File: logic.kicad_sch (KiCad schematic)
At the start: 38 parts, among them J2 TC2030, J5 Conn_01x04_Pin, J8 Conn_01x04, J9 Conn_01x04, SW1 SW_Push, SW2 SW_Push, U2 SN65HVD230, U4 HT753-1, U6 STM32F103C8Tx, Y1 8M

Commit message: schem: update 6n conn tvs diodes
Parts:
- removed D8, D9: H5VU10U, GLCS:Diode_DFN1006, symbol GLCS:H5VU10U
- added D17, D18: SMBJ6.0CA, Diode_SMD:D_SMA, symbol Device:D_TVS
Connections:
- net +5V: now also D17.1 (A1), D18.1 (A1)
- net GND: now also D17.2 (A2), D18.2 (A2)

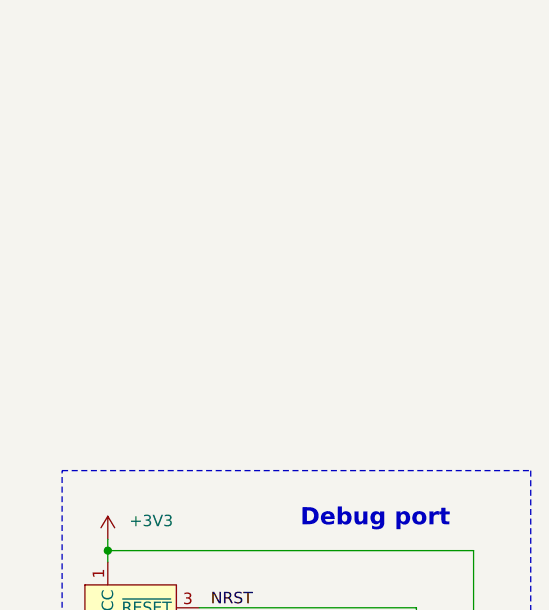
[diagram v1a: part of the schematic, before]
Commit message: schem: add rgb status led
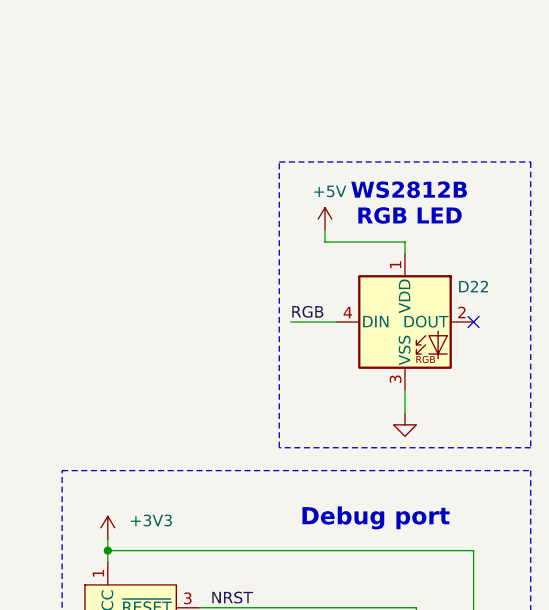
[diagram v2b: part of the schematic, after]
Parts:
- added D22: WS2812B, LED_SMD:LED_WS2812B_PLCC4_5.0x5.0mm_P3.2mm, symbol LED:WS2812B
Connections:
- net +5V: now also D22.1 (VDD)
- net GND: now also D22.3 (VSS)
- new net RGB: D22.4 (DIN)
- no-connect marks 3 -> 4
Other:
- note added: "WS2812B RGB LED"

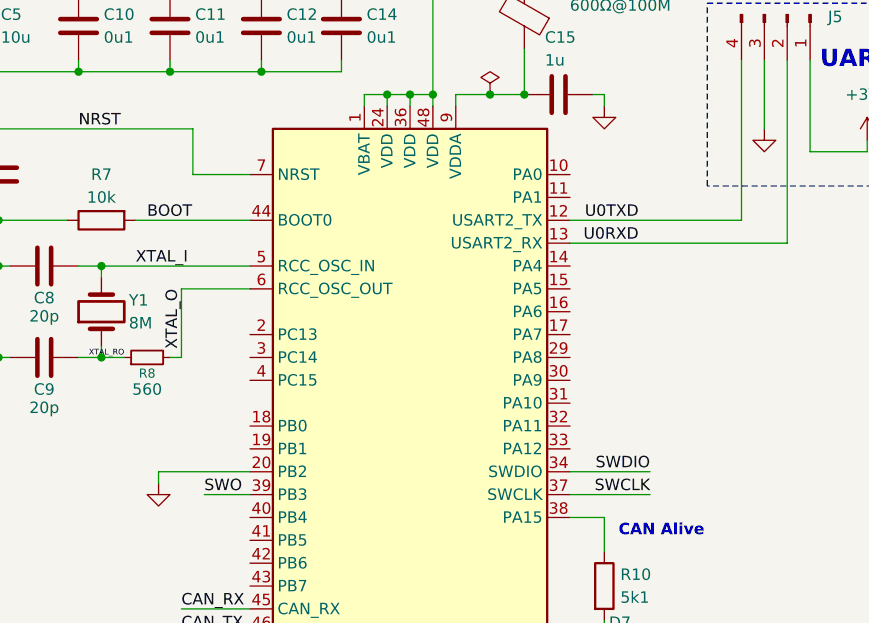
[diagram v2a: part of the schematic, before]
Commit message: schem: connect efuses to mcu
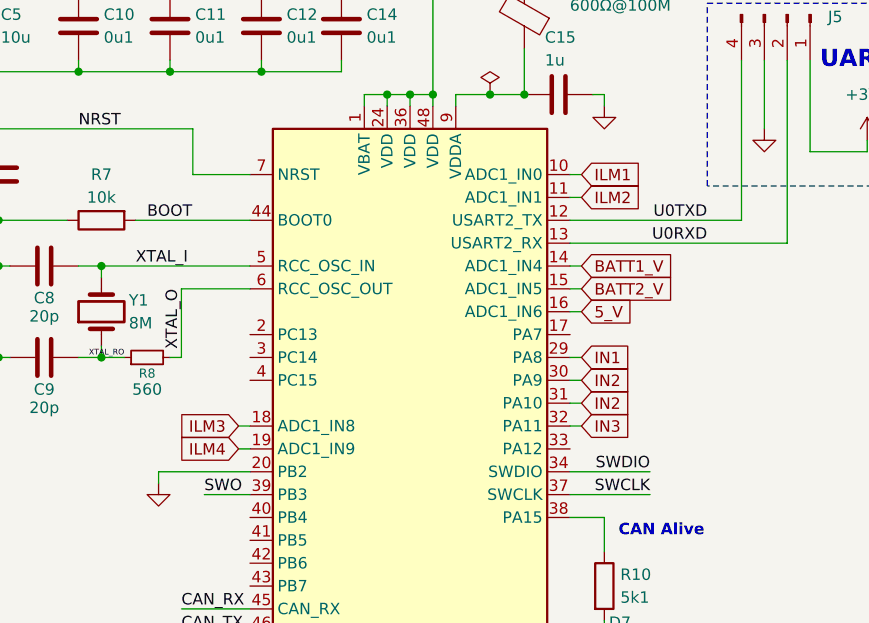
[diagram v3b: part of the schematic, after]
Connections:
- net ILM1: now reaches U6.10 (PA0)
- net ILM2: now reaches U6.11 (PA1)
- net BATT1_V: now reaches U6.14 (PA4)
- net BATT2_V: now reaches U6.15 (PA5)
- net 5_V: now reaches U6.16 (PA6)
- net ILM3: now reaches U6.18 (PB0)
- net ILM4: now reaches U6.19 (PB1)
- net IN1: now reaches U6.29 (PA8)
- net IN2: now reaches U6.30 (PA9)
- net IN2: now also U6.31 (PA10)
- net IN3: now reaches U6.32 (PA11)

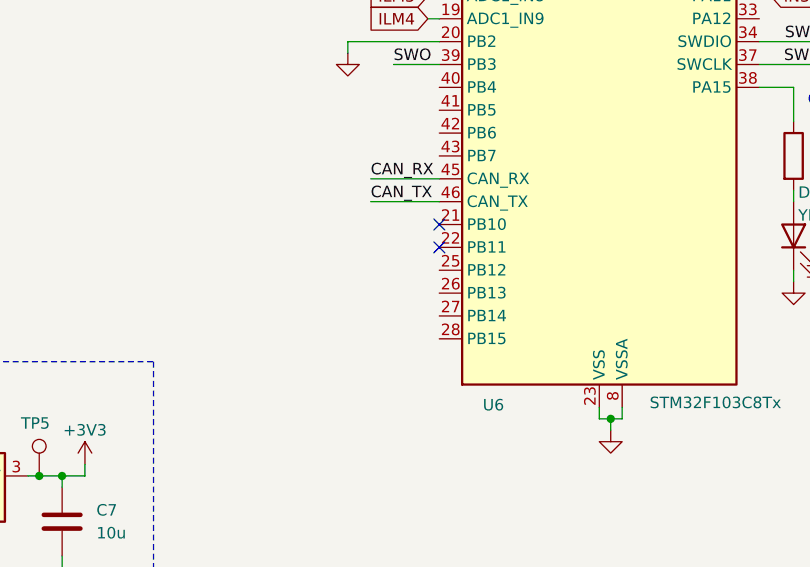
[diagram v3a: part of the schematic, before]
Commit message: schem: add test points
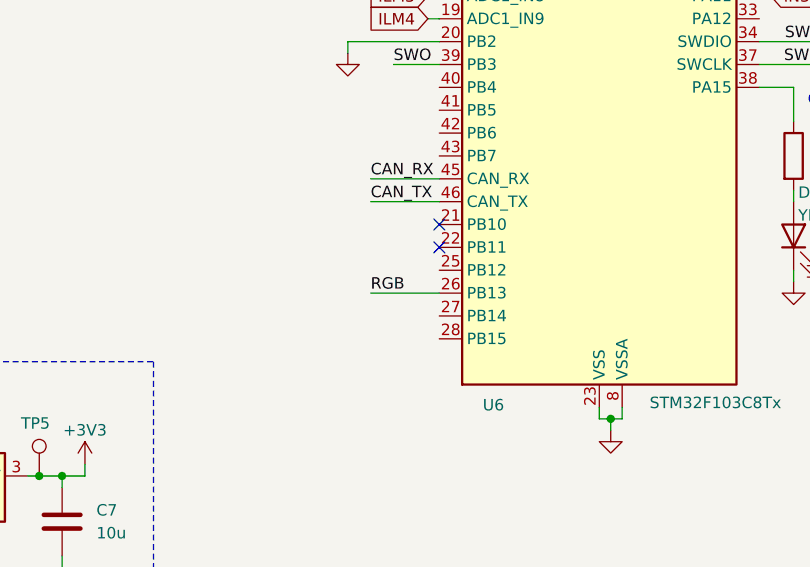
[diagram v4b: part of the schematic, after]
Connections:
- net RGB: now also U6.26 (PB13)
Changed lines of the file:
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@@
+	(wire
+		(pts
+			(xy 116.84 123.19) (xy 124.46 123.19)
+		)
+		(stroke
+			(width 0)
+			(type default)
+		)
+	)
 	(wire
 		(pts
@@
 		)
 	)
+	(label "RGB"
+		(at 116.84 123.19 0)
+		(effects
+			(font
+				(size 1.27 1.27)
+			)
+			(justify left bottom)
+		)
+	)

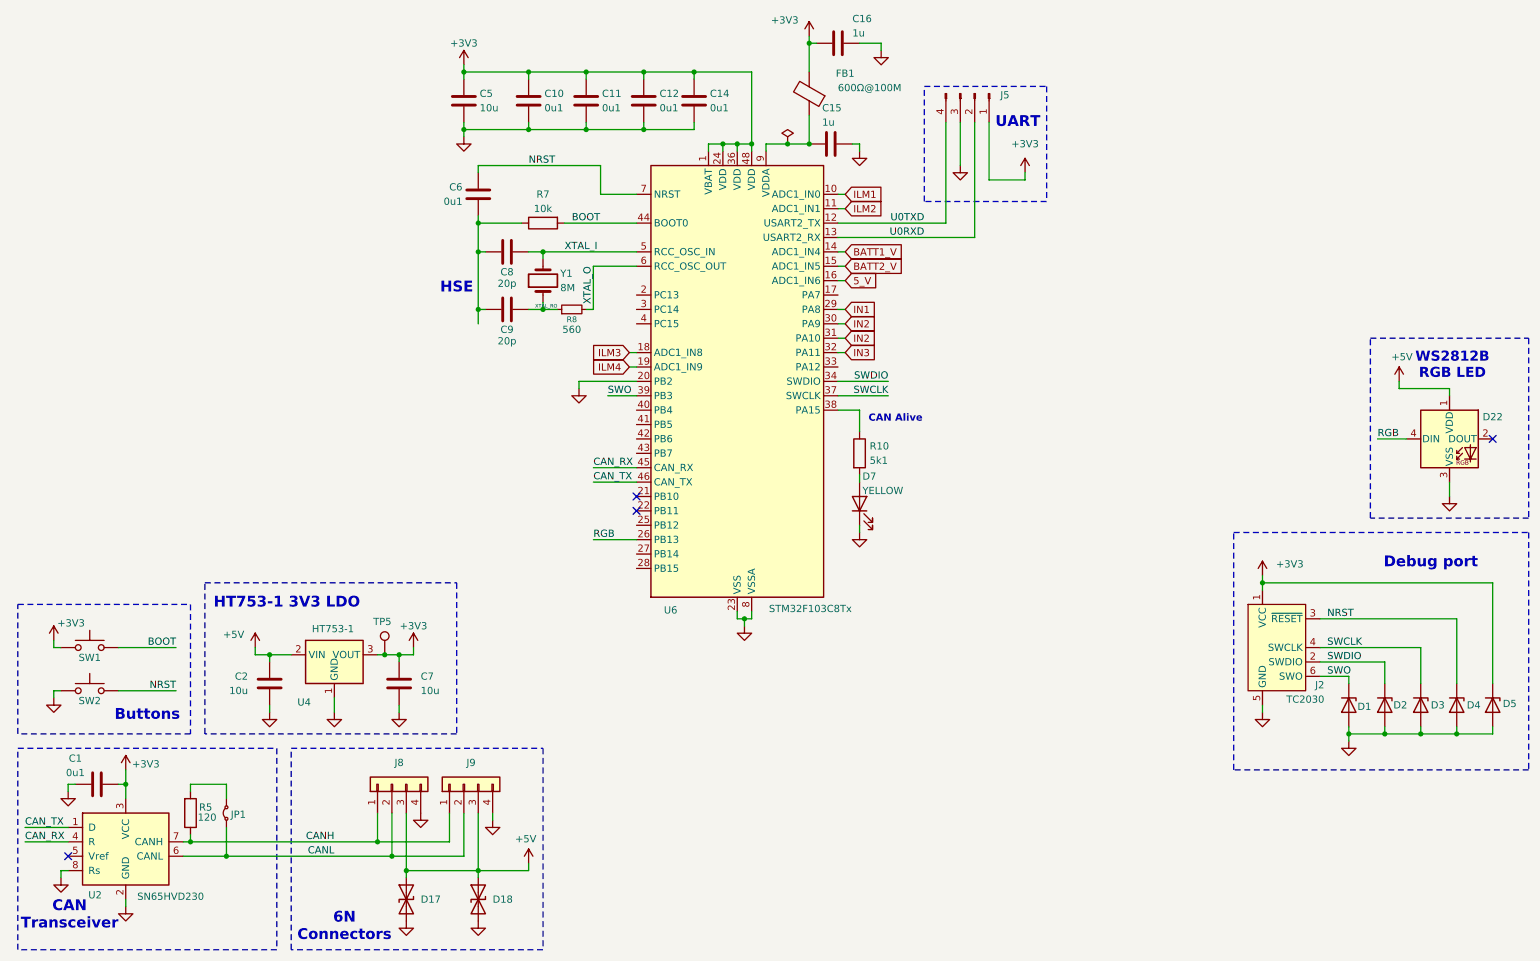
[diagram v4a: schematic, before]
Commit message: schem: add current measure jumpers
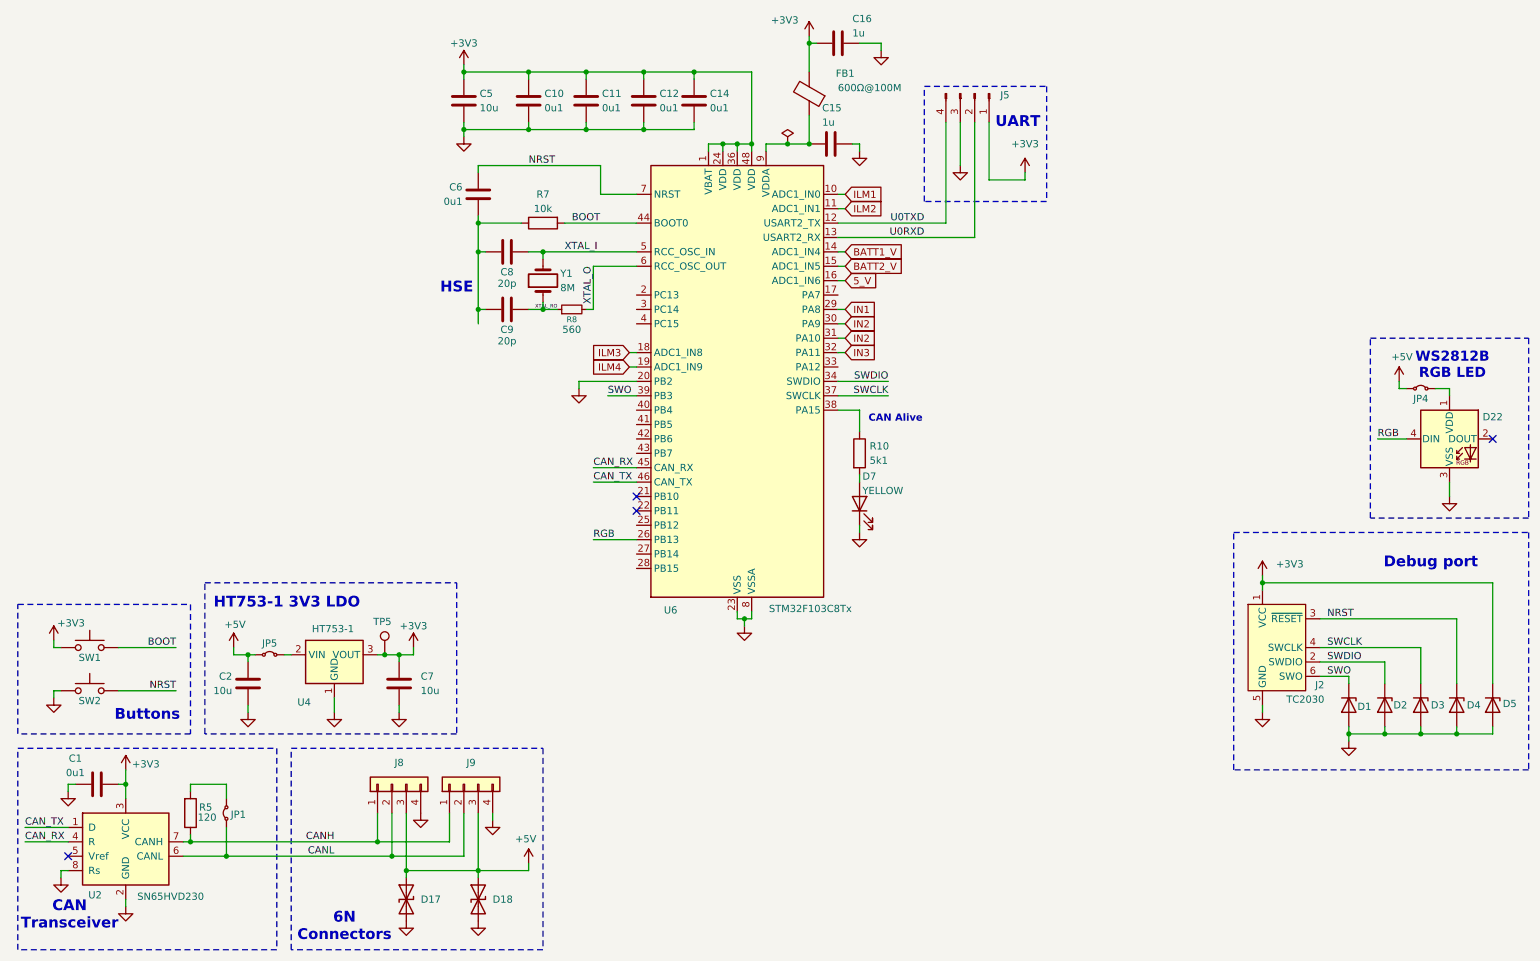
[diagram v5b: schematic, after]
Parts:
- added JP4, JP5: Jumper_2_Small_Bridged, Connector_PinHeader_2.54mm:PinHeader_1x02_P2.54mm_Vertical, symbol Jumper:Jumper_2_Small_Bridged
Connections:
- net +5V: now also JP4.1 (A), JP5.1 (A); no longer D22.1 (VDD), U4.2 (VIN)
- new net: D22.1 (VDD), JP4.2 (B)
- new net: JP5.2 (B), U4.2 (VIN)
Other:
- moved on the sheet: C2
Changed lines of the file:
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@@
 	)
 	(junction
-		(at 59.69 143.51)
+		(at 55.88 143.51)
 		(diameter 0)
 		(color 0 0 0 0)
@@
 	(wire
 		(pts
-			(xy 57.15 142.24) (xy 57.15 143.51)
+			(xy 53.34 142.24) (xy 53.34 143.51)
 		)
 		(stroke
@@
 	(wire
 		(pts
+			(xy 265.43 96.52) (xy 267.97 96.52)
+		)
+		(stroke
+			(width 0)
+			(type default)
+		)
+	)
+	(wire
+		(pts
 			(xy 118.11 62.23) (xy 118.11 57.15)
 		)
@@
 	(wire
 		(pts
-			(xy 59.69 143.51) (xy 59.69 144.78)
+			(xy 55.88 143.51) (xy 55.88 144.78)
 		)
 		(stroke
@@
 	(wire
 		(pts
+			(xy 62.23 143.51) (xy 63.5 143.51)
+		)
+		(stroke
+			(width 0)
+			(type default)
+		)
+	)
+	(wire
+		(pts
 			(xy 34.29 163.83) (xy 34.29 166.37)
 		)
@@
 	(wire
 		(pts
-			(xy 259.08 96.52) (xy 267.97 96.52)
+			(xy 259.08 96.52) (xy 260.35 96.52)
 		)
 		(stroke
@@
 	(wire
 		(pts
-			(xy 59.69 152.4) (xy 59.69 153.67)
+			(xy 55.88 152.4) (xy 55.88 153.67)
 		)
 		(stroke
@@
 	(wire
 		(pts
-			(xy 59.69 143.51) (xy 63.5 143.51)
+			(xy 55.88 143.51) (xy 57.15 143.51)
 		)
 		(stroke
@@
 	(wire
 		(pts
-			(xy 57.15 143.51) (xy 59.69 143.51)
+			(xy 53.34 143.51) (xy 55.88 143.51)
 		)
 		(stroke
@@
 	(symbol
 		(lib_id "power:GND")
-		(at 59.69 153.67 0)
+		(at 55.88 153.67 0)
 		(unit 1)
 		(body_style 1)
@@
 		(fields_autoplaced yes)
 		(property "Reference" "#PWR017"
-			(at 59.69 160.02 0)
+			(at 55.88 160.02 0)
 			(hide yes)
 			(show_name no)
@@
 		)
 		(property "Value" "GND"
-			(at 59.69 158.75 0)
+			(at 55.88 158.75 0)
 			(hide yes)
 			(show_name no)
@@
 		)
 		(property "Footprint" ""
-			(at 59.69 153.67 0)
+			(at 55.88 153.67 0)
 			(hide yes)
 			(show_name no)
@@
 		)
 		(property "Datasheet" ""
-			(at 59.69 153.67 0)
+			(at 55.88 153.67 0)
 			(hide yes)
 			(show_name no)
@@
 		)
 		(property "Description" "Power symbol creates a global label with name \"GND\" , ground"
-			(at 59.69 153.67 0)
+			(at 55.88 153.67 0)
 			(hide yes)
 			(show_name no)
@@
 	)
 	(symbol
+		(lib_name "Jumper_2_Small_Bridged_1")
+		(lib_id "Jumper:Jumper_2_Small_Bridged")
+		(at 262.89 96.52 0)
+		(unit 1)
+		(body_style 1)
+		(exclude_from_sim no)
+		(in_bom yes)
+		(on_board yes)
+		(in_pos_files yes)
+		(dnp no)
+		(property "Reference" "JP4"
+			(at 262.89 98.298 0)
+			(show_name no)
+			(do_not_autoplace no)
+			(effects
+				(font
+					(size 1.27 1.27)
+				)
+			)
+		)
+		(property "Value" "Jumper_2_Small_Bridged"
+			(at 262.89 93.98 0)
+			(hide yes)
+			(show_name no)
+			(do_not_autoplace no)
+			(effects
+				(font
+					(size 1.27 1.27)
+				)
+			)
+		)
+		(property "Footprint" "Connector_PinHeader_2.54mm:PinHeader_1x02_P2.54mm_Vertical"
+			(at 262.89 96.52 0)
+			(hide yes)
+			(show_name no)
+			(do_not_autoplace no)
+			(effects
+				(font
+					(size 1.27 1.27)
+				)
+			)
+		)
+		(property "Datasheet" ""
+			(at 262.89 96.52 0)
+			(hide yes)
+			(show_name no)
+			(do_not_autoplace no)
+			(effects
+				(font
+					(size 1.27 1.27)
+				)
+			)
+		)
+		(property "Description" "Jumper, 2-pole, small symbol, bridged"
+			(at 262.89 96.52 0)
+			(hide yes)
+			(show_name no)
+			(do_not_autoplace no)
+			(effects
+				(font
+					(size 1.27 1.27)
+				)
+			)
+		)
+		(pin "2"
+		)
+		(pin "1"
+		)
+		(instances
+			(project "s6tm-detect-psu-1"
+				(path "/c28e80f1-f767-484a-bf96-16c1e8738b05/a8ebaca3-da9e-4a0a-a7e6-414b19783be9"
+					(reference "JP4")
+					(unit 1)
+				)
+			)
+		)
+	)
+	(symbol
 		(lib_id "Interface_CAN_LIN:SN65HVD230")
 		(at 34.29 176.53 0)
@@
 	)
 	(symbol
+		(lib_name "Jumper_2_Small_Bridged_2")
+		(lib_id "Jumper:Jumper_2_Small_Bridged")
+		(at 59.69 143.51 0)
+		(unit 1)
+		(body_style 1)
+		(exclude_from_sim no)
+		(in_bom yes)
+		(on_board yes)
+		(in_pos_files yes)
+		(dnp no)
+		(property "Reference" "JP5"
+			(at 59.69 141.478 0)
+			(show_name no)
+			(do_not_autoplace no)
+			(effects
+				(font
+					(size 1.27 1.27)
+				)
+			)
+		)
+		(property "Value" "Jumper_2_Small_Bridged"
+			(at 59.69 140.97 0)
+			(hide yes)
+			(show_name no)
+			(do_not_autoplace no)
+			(effects
+				(font
+					(size 1.27 1.27)
+				)
+			)
+		)
+		(property "Footprint" "Connector_PinHeader_2.54mm:PinHeader_1x02_P2.54mm_Vertical"
+			(at 59.69 143.51 0)
+			(hide yes)
+			(show_name no)
+			(do_not_autoplace no)
+			(effects
+				(font
+					(size 1.27 1.27)
+				)
+			)
+		)
+		(property "Datasheet" ""
+			(at 59.69 143.51 0)
+			(hide yes)
+			(show_name no)
+			(do_not_autoplace no)
+			(effects
+				(font
+					(size 1.27 1.27)
+				)
+			)
+		)
+		(property "Description" "Jumper, 2-pole, small symbol, bridged"
+			(at 59.69 143.51 0)
+			(hide yes)
+			(show_name no)
+			(do_not_autoplace no)
+			(effects
+				(font
+					(size 1.27 1.27)
+				)
+			)
+		)
+		(pin "2"
+		)
+		(pin "1"
+		)
+		(instances
+			(project "s6tm-detect-psu-1"
+				(path "/c28e80f1-f767-484a-bf96-16c1e8738b05/a8ebaca3-da9e-4a0a-a7e6-414b19783be9"
+					(reference "JP5")
+					(unit 1)
+				)
+			)
+		)
+	)
+	(symbol
 		(lib_id "MCU_ST_STM32F1:STM32F103C8Tx")
 		(at 142.24 95.25 0)
@@
 	(symbol
 		(lib_id "Device:C")
-		(at 59.69 148.59 0)
+		(at 55.88 148.59 0)
 		(mirror y)
 		(unit 1)
@@
 		(dnp no)
 		(property "Reference" "C2"
-			(at 55.88 147.3199 0)
+			(at 53.086 147.32 0)
 			(show_name no)
 			(do_not_autoplace no)
@@
 		)
 		(property "Value" "10u"
-			(at 55.88 149.8599 0)
+			(at 53.086 149.86 0)
 			(show_name no)
 			(do_not_autoplace no)
@@
 		)
 		(property "Footprint" "Capacitor_SMD:C_0805_2012Metric"
-			(at 58.7248 152.4 0)
+			(at 54.9148 152.4 0)
 			(hide yes)
 			(show_name no)
@@
 		)
 		(property "Datasheet" ""
-			(at 59.69 148.59 0)
+			(at 55.88 148.59 0)
 			(hide yes)
 			(show_name no)
@@
 		)
 		(property "Description" "Unpolarized capacitor"
-			(at 59.69 148.59 0)
+			(at 55.88 148.59 0)
 			(hide yes)
 			(show_name no)
@@
 		)
 		(property "Basic" "Y"
-			(at 59.69 148.59 0)
+			(at 55.88 148.59 0)
 			(hide yes)
 			(show_name no)
@@
 		)
 		(property "JLCPCB Part #" "C440198"
-			(at 59.69 148.59 0)
+			(at 55.88 148.59 0)
 			(hide yes)
 			(show_name no)
@@
 		)
 		(property "Manufacturer" "Murata"
-			(at 59.69 148.59 0)
+			(at 55.88 148.59 0)
 			(hide yes)
 			(show_name no)
@@
 		)
 		(property "Manufacturer Part Number" "GRM21BR61H106KE43L"
-			(at 59.69 148.59 0)
+			(at 55.88 148.59 0)
 			(hide yes)
 			(show_name no)
@@
 	(symbol
 		(lib_id "power:+5V")
-		(at 57.15 142.24 0)
+		(at 53.34 142.24 0)
 		(unit 1)
 		(body_style 1)
@@
 		(dnp no)
 		(property "Reference" "#PWR016"
-			(at 57.15 146.05 0)
+			(at 53.34 146.05 0)
 			(hide yes)
 			(show_name no)
@@
 		)
 		(property "Value" "+5V"
-			(at 53.34 139.954 0)
+			(at 53.594 138.176 0)
 			(show_name no)
 			(do_not_autoplace no)
@@
 		)
 		(property "Footprint" ""
-			(at 57.15 142.24 0)
+			(at 53.34 142.24 0)
 			(hide yes)
 			(show_name no)
@@
 		)
 		(property "Datasheet" ""
-			(at 57.15 142.24 0)
+			(at 53.34 142.24 0)
 			(hide yes)
 			(show_name no)
@@
 		)
 		(property "Description" "Power symbol creates a global label with name \"+5V\""
-			(at 57.15 142.24 0)
+			(at 53.34 142.24 0)
 			(hide yes)
 			(show_name no)

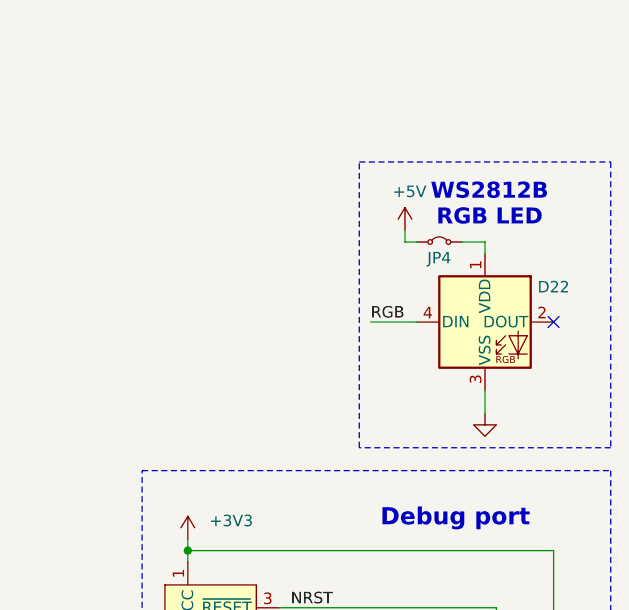
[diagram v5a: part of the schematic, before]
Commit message: schem: add rgb decoupling cap
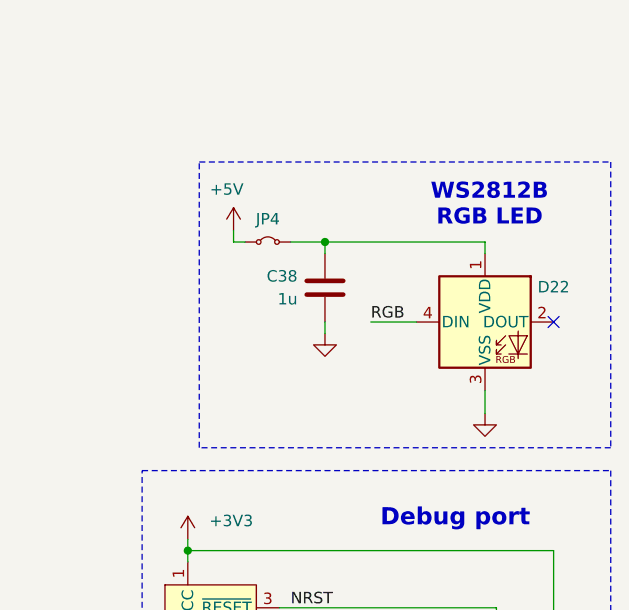
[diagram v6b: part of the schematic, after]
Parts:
- added C38: 1u, Capacitor_SMD:C_0402_1005Metric, symbol Device:C
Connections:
- net GND: now also C38.1
- net at D22.1 (VDD), JP4.2 (B): now also C38.2
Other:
- moved on the sheet: JP4
